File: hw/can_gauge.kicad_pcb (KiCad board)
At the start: 2 copper layers, 27 parts, among them J1 Gauge 1, J2 Gauge 2, J3 Gauge 3, J4 Gauge 4, J5 Gauge 5, J6 Power and CAN, U1 PIC16F1459-ISS, U2 MCP2515-xST, U3 MCP2561T-E/SN, U4 74HC595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

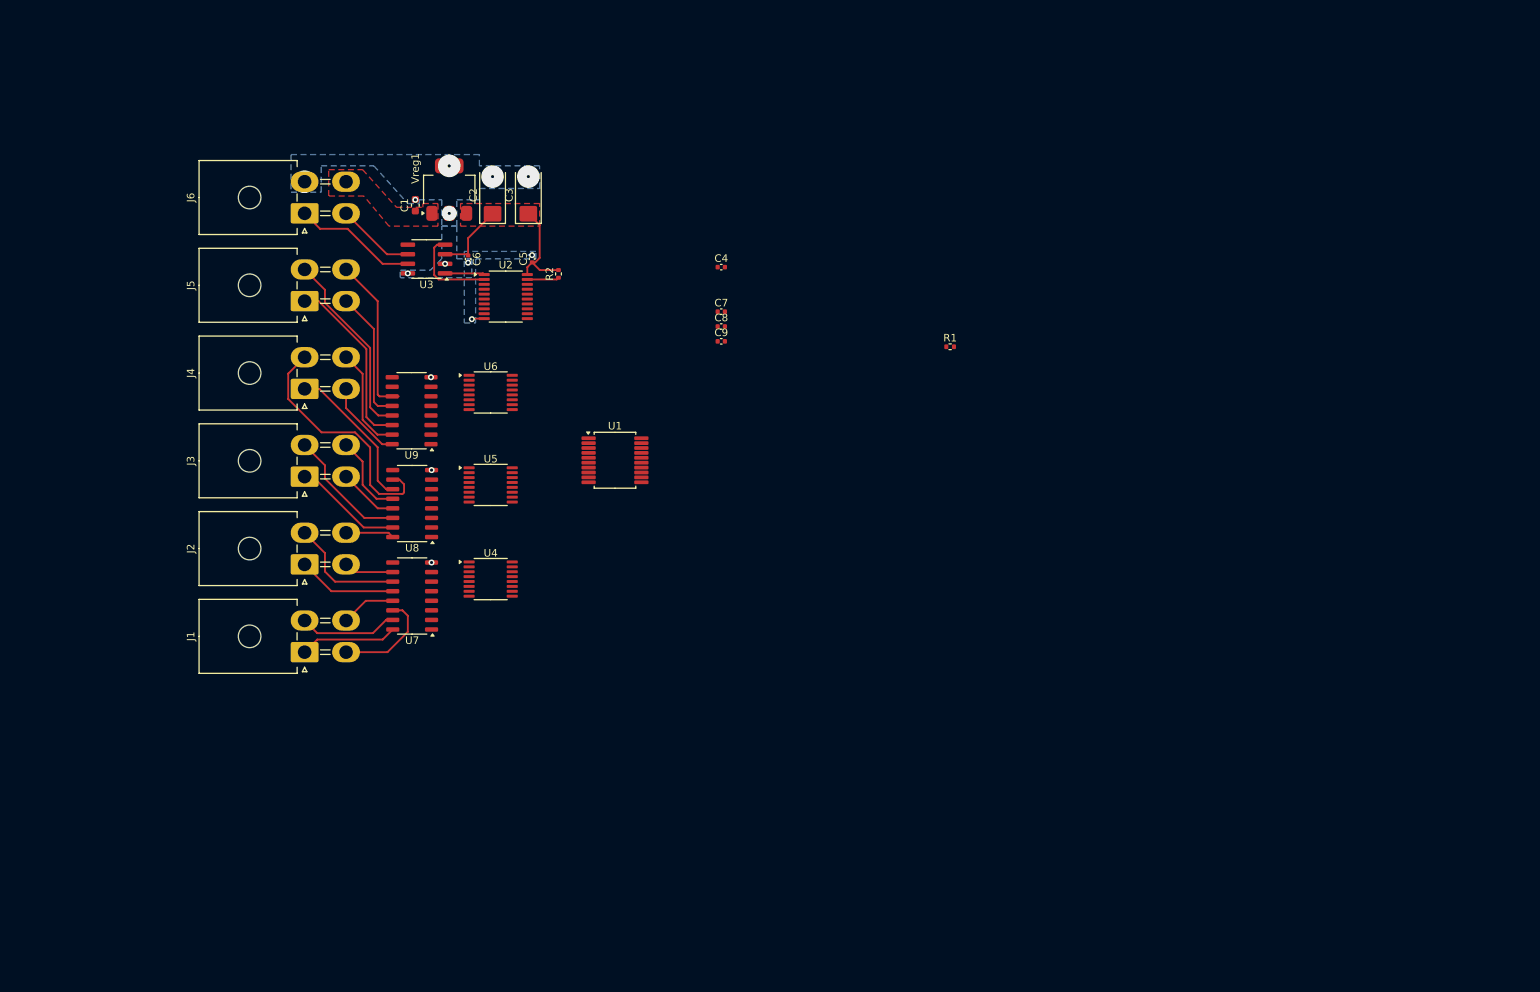
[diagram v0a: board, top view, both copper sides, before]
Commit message: hw: change connector layout
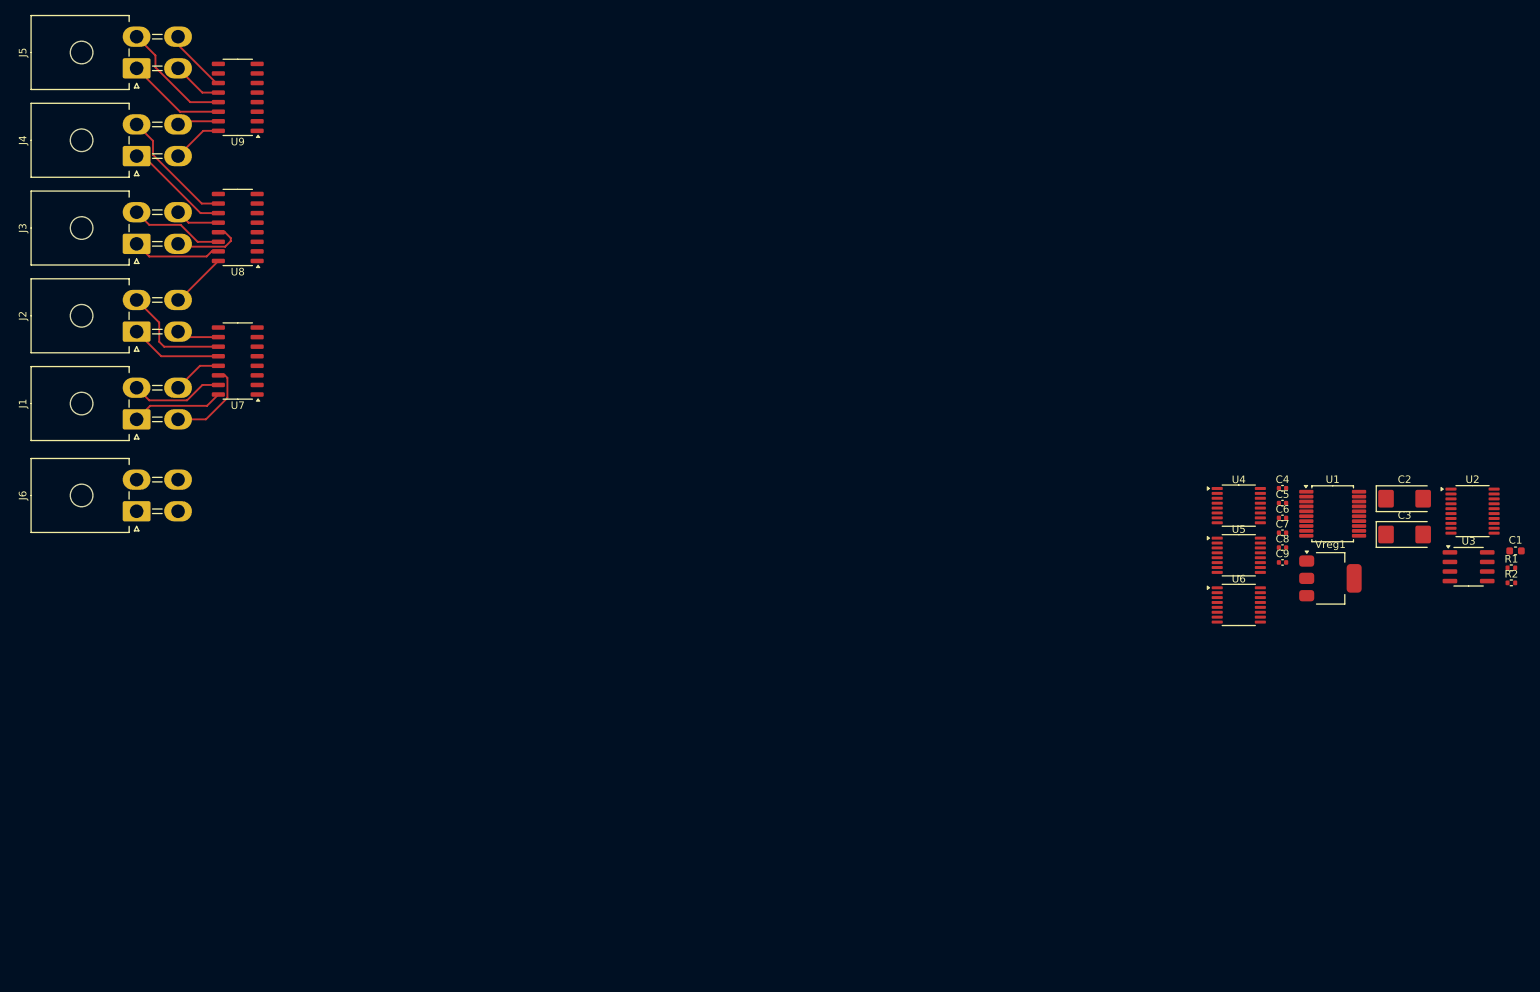
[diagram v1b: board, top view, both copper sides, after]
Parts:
- J6: value Power and CAN -> Power & CAN
- moved C1 153.1 mm to (225.0, 102.3), turned to 0 degrees
- moved U3 144.2 mm to (218.8, 104.4), turned to 0 degrees
- moved R2 133.0 mm to (224.5, 106.5), turned to 0 degrees
- moved U2 131.5 mm to (219.3, 97.0)
- moved Vreg1 127.8 mm to (200.5, 105.9), turned to 0 degrees
- moved C2 127.6 mm to (210.3, 95.3), turned to 0 degrees
- moved C3 124.7 mm to (210.3, 100.1), turned to 0 degrees
- moved C6 113.4 mm to (194.1, 97.9), turned to 0 degrees
- moved C5 104.8 mm to (194.1, 95.9), turned to 0 degrees
- moved U6 103.2 mm to (188.3, 109.4)
- moved U4 99.8 mm to (188.3, 96.2)
- moved U5 99.7 mm to (188.3, 102.8)
- moved U1 95.5 mm to (200.8, 97.3)
- moved C4 80.1 mm to (194.1, 93.9)
- moved C7 80.1 mm to (194.1, 99.8)
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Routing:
- net +5V: track 23.5 -> 0.00 mm
- net M4P2: track 32.9 -> 16.3 mm
- net CAN_H: track 16.5 -> 0.00 mm
- net M5P4: track 21.2 -> 8.53 mm
- net RX: track 12.3 -> 0.00 mm
- net M5P3: track 17.6 -> 6.68 mm
- net M5P1: track 23.7 -> 13.2 mm
- net CAN_L: track 10.4 -> 0.00 mm
- net M5P2: track 25.3 -> 15.4 mm
- net M4P4: track 14.0 -> 5.52 mm
- net M3P4: track 12.2 -> 5.93 mm
- net M4P1: track 19.8 -> 14.0 mm
- net TX: track 5.25 -> 0.00 mm
- net M3P2: track 16.7 -> 12.5 mm
- net Net-(U2-~{RESET}): track 4.23 -> 0.00 mm
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- removed copper zone on F.Cu, net +12V
- removed copper zone on F.Cu, net +5V
- removed copper zone on B.Cu, net GND

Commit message: hw: 8-way transistor arrays, 6 gauges
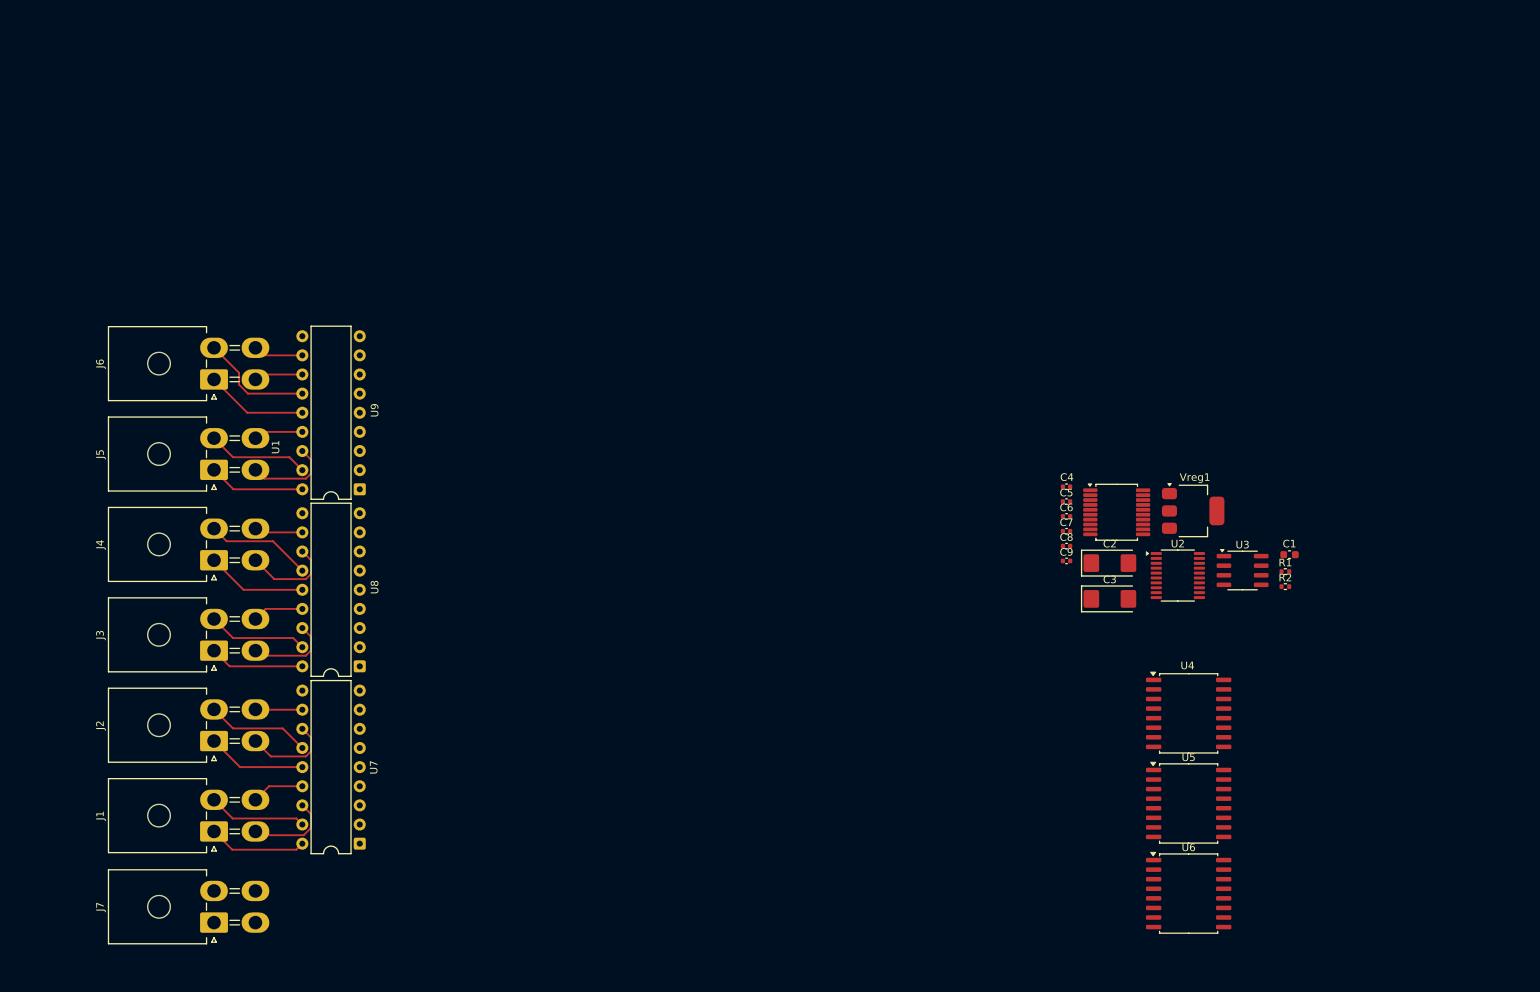
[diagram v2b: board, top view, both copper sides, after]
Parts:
- added J7: Power & CAN, Connector_Molex:Molex_Mini-Fit_Jr_5569-04A2_2x02_P4.20mm_Horizontal, F.Cu at (52.3, 151.6)
- J6: value Power & CAN -> Gauge 6
- U4, U5, U6: footprint Package_SO:TSSOP-16_4.4x5mm_P0.65mm -> Package_SO:SOIC-16W_7.5x10.3mm_P1.27mm
- U7, U8, U9: value ULN2003A -> ULN2804A; footprint Package_SO:SO-16_3.9x9.9mm_P1.27mm -> Package_DIP:DIP-18_W7.62mm
- moved U7 66.1 mm to (71.6, 141.1)
- moved U8 60.5 mm to (71.6, 117.6)
- moved J1 55.7 mm to (52.3, 139.5)
- moved J2 55.3 mm to (52.3, 127.5)
- moved J3 55.0 mm to (52.3, 115.5)
- moved J4 54.6 mm to (52.3, 103.5)
- moved U9 54.5 mm to (71.6, 94.1)
- moved J5 54.3 mm to (52.3, 91.5)
- moved C2 40.0 mm to (171.2, 103.9)
- moved C3 40.0 mm to (171.2, 108.6)
- moved U2 40.0 mm to (180.2, 105.5)
- moved U6 38.9 mm to (181.7, 147.7)
- moved U5 33.6 mm to (181.7, 135.8)
- moved C1 30.0 mm to (195.0, 102.8)
- moved R1 30.0 mm to (194.5, 105.0)
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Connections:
- J6 pad 1: CAN_H -> M6P1
- J6 pad 2: GND -> M6P2
- J6 pad 3: CAN_L -> M6P3
- J6 pad 4: +12V -> M6P4
- U6 pad 4: unconnected-(U6-QE-Pad4) -> Net-(U6-QE)
- U6 pad 5: unconnected-(U6-QF-Pad5) -> Net-(U6-QF)
- U6 pad 6: unconnected-(U6-QG-Pad6) -> Net-(U6-QG)
- U6 pad 7: unconnected-(U6-QH-Pad7) -> Net-(U6-QH)
- U7 pad 10: M2P3 -> +5V
- U7 pad 11: M2P2 -> M2P4
- U7 pad 12: M2P1 -> M2P3
- U7 pad 13: M1P4 -> M2P2
- U7 pad 14: M1P3 -> M2P1
- U7 pad 15: M1P2 -> M1P4
- U7 pad 16: M1P1 -> M1P3
- U7 pad 8: GND -> Net-(U4-QH)
- U7 pad 9: +5V -> GND
- U8 pad 1: Net-(U4-QH) -> Net-(U5-QA)
- U8 pad 10: M4P2 -> +5V
- U8 pad 11: M4P1 -> M4P4
- U8 pad 12: M3P4 -> M4P3
- U8 pad 13: M3P3 -> M4P2
- U8 pad 14: M3P2 -> M4P1
- U8 pad 15: M3P1 -> M3P4
- U8 pad 16: M2P4 -> M3P3
- U8 pad 2: Net-(U5-QA) -> Net-(U5-QB)
- U8 pad 3: Net-(U5-QB) -> Net-(U5-QC)
- U8 pad 4: Net-(U5-QC) -> Net-(U5-QD)
- U8 pad 5: Net-(U5-QD) -> Net-(U5-QE)
- U8 pad 6: Net-(U5-QE) -> Net-(U5-QF)
- U8 pad 7: Net-(U5-QF) -> Net-(U5-QG)
- U8 pad 8: GND -> Net-(U5-QH)
- U8 pad 9: +5V -> GND
- U9 pad 1: Net-(U5-QG) -> Net-(U6-QA)
- U9 pad 10: unconnected-(U9-O7-Pad10) -> +5V
- U9 pad 11: M5P4 -> M6P4
- U9 pad 12: M5P3 -> M6P3
- U9 pad 13: M5P2 -> M6P2
- U9 pad 14: M5P1 -> M6P1
- U9 pad 15: M4P4 -> M5P4
- U9 pad 16: M4P3 -> M5P3
- U9 pad 2: Net-(U5-QH) -> Net-(U6-QB)
- U9 pad 3: Net-(U6-QA) -> Net-(U6-QC)
- U9 pad 4: Net-(U6-QB) -> Net-(U6-QD)
- U9 pad 5: Net-(U6-QC) -> Net-(U6-QE)
- U9 pad 6: Net-(U6-QD) -> Net-(U6-QF)
- U9 pad 7: unconnected-(U9-I7-Pad7) -> Net-(U6-QG)
- U9 pad 8: GND -> Net-(U6-QH)
- U9 pad 9: +5V -> GND
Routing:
- net M6P2: track 0.00 -> 15.2 mm
- net M6P1: track 0.00 -> 13.6 mm
- net M6P4: track 0.00 -> 6.64 mm
- net M6P3: track 0.00 -> 6.50 mm
- net M2P3: track 5.65 -> 11.9 mm
- net M4P3: track 6.74 -> 12.1 mm
- net M5P3: track 6.68 -> 11.6 mm
- net M4P2: track 16.3 -> 14.0 mm
- net M5P4: track 8.53 -> 6.57 mm
- net M5P2: track 15.4 -> 13.5 mm
- net M3P3: track 9.83 -> 11.4 mm
- net M2P4: track 7.50 -> 6.24 mm
- net M2P2: track 14.9 -> 13.8 mm
- net M2P1: track 12.2 -> 13.2 mm
- net M4P4: track 5.52 -> 6.43 mm
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
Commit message: hw: shift register placement
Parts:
- moved U6 119.8 mm to (80.5, 83.5)
- moved U5 105.2 mm to (80.5, 107.0)
- moved U4 101.4 mm to (80.5, 131.0)
- moved C7 83.6 mm to (87.0, 128.5), turned to -90 degrees
- moved C9 81.6 mm to (87.0, 81.0), turned to -90 degrees
- moved C8 78.5 mm to (87.0, 104.5), turned to -90 degrees
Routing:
- net +5V: track 0.00 -> 103.6 mm
- net Net-(U4-QH'): track 0.00 -> 37.9 mm
- net Net-(U5-QH'): track 0.00 -> 37.4 mm
- net Net-(U4-QA): track 0.00 -> 21.7 mm
- net Net-(U6-QA): track 0.00 -> 21.7 mm
- net Net-(U5-QA): track 0.00 -> 21.4 mm
- net Net-(U4-QB): track 0.00 -> 20.4 mm
- net Net-(U5-QB): track 0.00 -> 20.2 mm
- net Net-(U6-QB): track 0.00 -> 20.2 mm
- net Net-(U4-QH): track 0.00 -> 17.0 mm
- net Net-(U5-QH): track 0.00 -> 16.9 mm
- net Net-(U6-QH): track 0.00 -> 16.8 mm
- net Net-(U5-QC): track 0.00 -> 14.3 mm
- net Net-(U4-QC): track 0.00 -> 14.1 mm
- net Net-(U6-QC): track 0.00 -> 13.8 mm
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- added copper zone on F.Cu, net +5V
- added copper zone on B.Cu, net GND

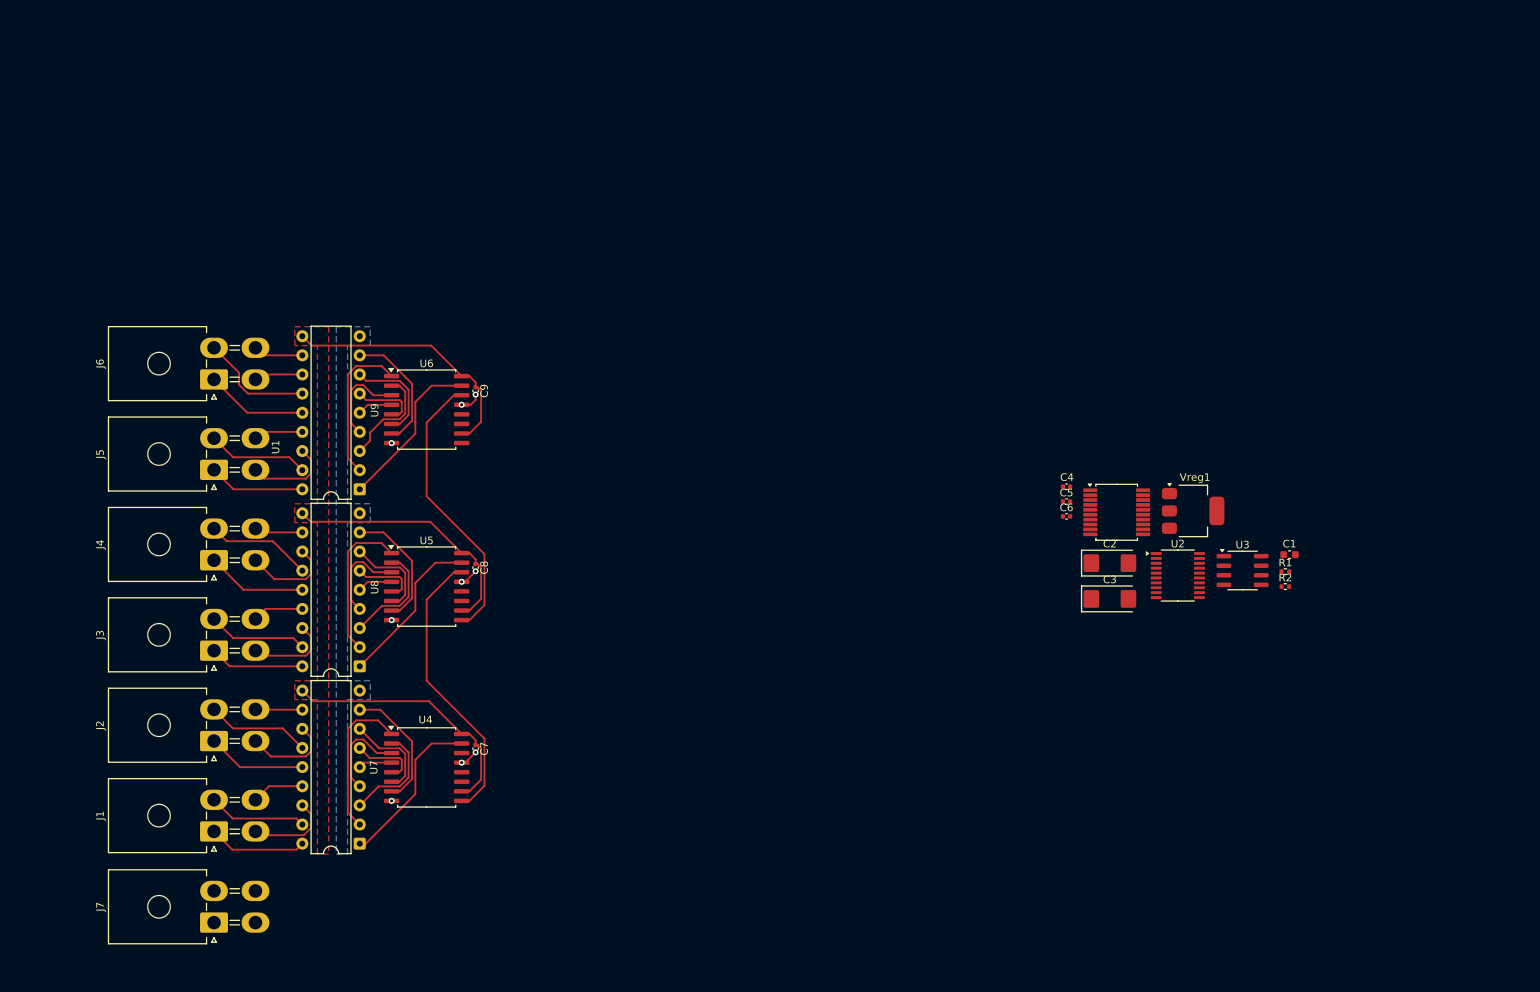
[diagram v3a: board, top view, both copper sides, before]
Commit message: hw: through-hole shift registers
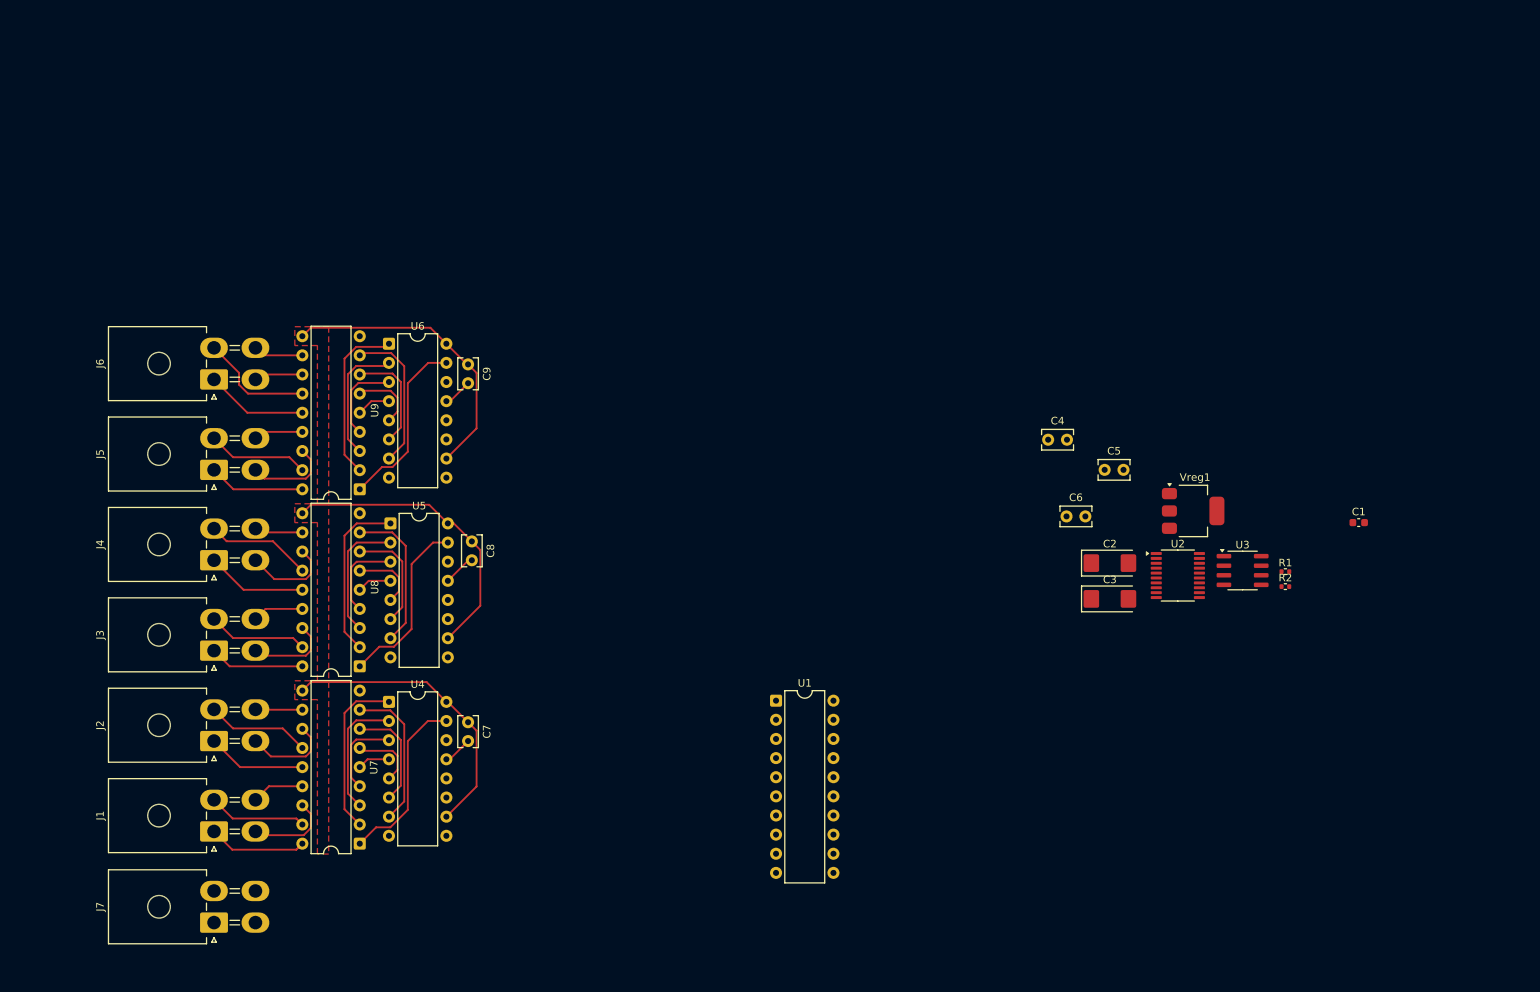
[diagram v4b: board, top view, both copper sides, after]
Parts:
- C4, C5, C6, C7, C8, C9: footprint Capacitor_SMD:C_0402_1005Metric -> Capacitor_THT:C_Rect_L4.0mm_W2.5mm_P2.50mm
- U1: value PIC16F1459-ISS -> PIC16F1459-IP; footprint Package_SO:SSOP-20_5.3x7.2mm_P0.65mm -> Package_DIP:DIP-20_W7.62mm
- U4, U5, U6: footprint Package_SO:SOIC-16W_7.5x10.3mm_P1.27mm -> Package_DIP:DIP-16_W7.62mm
- moved U1 51.7 mm to (126.9, 122.1)
- moved C1 10.1 mm to (204.2, 98.5)
- moved U6 10.1 mm to (75.5, 74.8)
- moved U4 10.0 mm to (75.5, 122.3)
- moved U5 9.67 mm to (75.7, 98.6)
- moved C4 6.70 mm to (163.0, 87.5)
- moved C5 6.58 mm to (170.5, 91.5)
- moved C7 3.66 mm to (86.0, 125.0)
- moved C9 3.66 mm to (86.0, 77.5)
- moved C8 3.52 mm to (86.5, 101.0)
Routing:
- net Net-(U4-QH'): track 37.9 -> 0.00 mm
- net Net-(U5-QH'): track 37.4 -> 0.00 mm
- net +5V: track 103.6 -> 118.5 mm
- net GND: track 7.69 -> 12.1 mm
- net Net-(U6-QC): track 13.8 -> 16.9 mm
- net Net-(U5-QH): track 16.9 -> 19.9 mm
- net Net-(U6-QH): track 16.8 -> 19.9 mm
- net Net-(U4-QH): track 17.0 -> 19.8 mm
- net Net-(U4-QC): track 14.1 -> 16.8 mm
- net Net-(U5-QC): track 14.3 -> 17.0 mm
- net Net-(U5-QB): track 20.2 -> 22.4 mm
- net Net-(U5-QG): track 12.3 -> 14.5 mm
- net Net-(U6-QB): track 20.2 -> 22.4 mm
- net Net-(U5-QA): track 21.4 -> 23.6 mm
- net Net-(U6-QA): track 21.7 -> 23.8 mm
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- removed copper zone on B.Cu, net GND
